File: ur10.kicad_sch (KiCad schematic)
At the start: 0 parts

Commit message: Draw schematic.
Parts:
- added C14: 22u/25V, Capacitor_SMD:C_0805_2012Metric_Pad1.18x1.45mm_HandSolder, symbol Device:C
- added D1, D3: 1N5819, Diode_SMD:D_SOD-123, symbol Diode:1N5819
- added D2: YELLOW, LED_SMD:LED_0805_2012Metric_Pad1.15x1.40mm_HandSolder, symbol Device:LED
- added H1, H2, H3, H4: M3, MountingHole:MountingHole_3.2mm_M3_Pad_Via, symbol Mechanical:MountingHole
- added J1: ~, symbol Connector:Screw_Terminal_01x06
- added J2: ~, TerminalBlock_4Ucon:TerminalBlock_4Ucon_1x03_P3.50mm_Horizontal, symbol Connector:Screw_Terminal_01x03
- added K1: TNA-2C-12-05-L, Relay_THT:Relay_DPDT_Schrack-RT2-FormC_RM5mm, symbol Relay:Relay_DPDT
- added Q1: AO3401A, Package_TO_SOT_SMD:SOT-23, symbol Transistor_FET:AO3401A
- added R1, R14: 1k, Resistor_SMD:R_0805_2012Metric_Pad1.20x1.40mm_HandSolder, symbol Device:R
- added R11: 10k, Resistor_SMD:R_0805_2012Metric_Pad1.20x1.40mm_HandSolder, symbol Device:R
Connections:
- new net: C14.1, D1.1 (K), Q1.2 (S), R11.1
- new net: Q1.1 (G), R11.2, R14.2
- new net: D2.1 (K), R1.2
- new net: D2.2 (A), D3.1 (K), K1.A1, Q1.3 (D)
- new net 11: J1.5 (Pin_5), K1.11
- new net 12: J1.4 (Pin_4), K1.12
- new net 14: J1.6 (Pin_6), K1.14
- new net 21: J1.2 (Pin_2), K1.21
- new net 22: J1.1 (Pin_1), K1.22
- new net 24: J1.3 (Pin_3), K1.24
- new net CONTROL: J2.3 (Pin_3), R14.1
- new net GND: C14.2, D3.2 (A), J2.2 (Pin_2), K1.A2, R1.1
- new net VCC: D1.2 (A), J2.1 (Pin_1)
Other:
- company: (none) -> Model Railroader Club Brno I – KMŽ Brno I – https://kmz-brno.cz/
- title: (none) -> UR-10 - Universal relay module

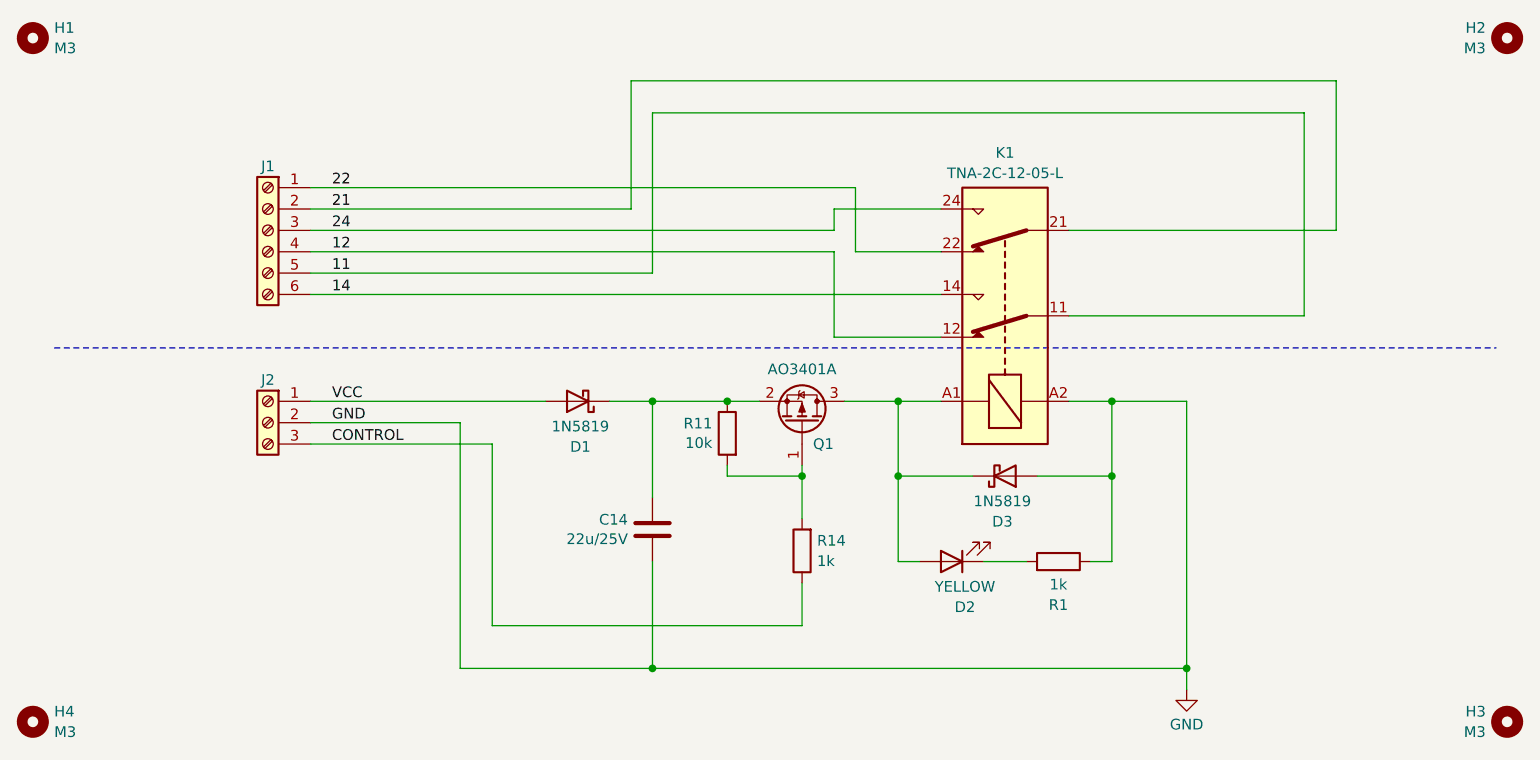
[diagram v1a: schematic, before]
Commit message: Add Q1 bypass, add polarity switch option.
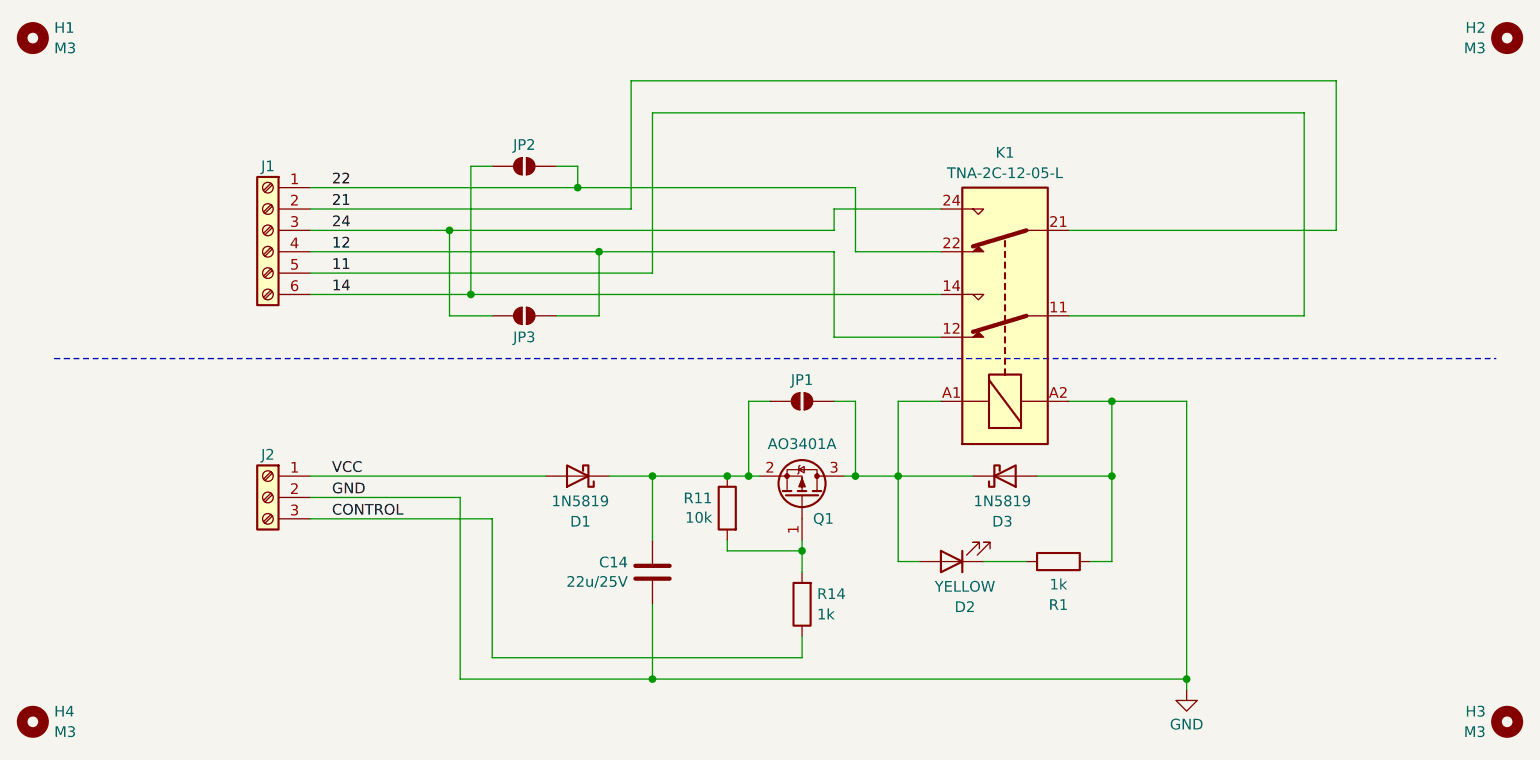
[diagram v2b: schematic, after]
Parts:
- added JP1, JP2, JP3: ~, symbol Jumper:SolderJumper_2_Open
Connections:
- net 12: now also JP3.2 (B)
- net 14: now also JP2.1 (A)
- net 22: now also JP2.2 (B)
- net 24: now also JP3.1 (A)
- net at C14.1, D1.1 (K), Q1.2 (S)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: now also JP1.1 (A)
- net at D2.2 (A), D3.1 (K), K1.A1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: now also JP1.2 (B)
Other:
- moved on the sheet: C14, D1, J2, Q1, R11, R14

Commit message: Wire PCB.
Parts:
- J1: footprint (none) -> TerminalBlock_Euroclamp:MVE252-5-V-3x
- JP1: renamed from JP2; footprint (none) -> Jumper:SolderJumper-2_P1.3mm_Open_RoundedPad1.0x1.5mm
- JP2: renamed from JP3; footprint (none) -> Jumper:SolderJumper-2_P1.3mm_Open_RoundedPad1.0x1.5mm
- JP3: renamed from JP1; footprint (none) -> Jumper:SolderJumper-2_P1.3mm_Open_RoundedPad1.0x1.5mm
- Q1: footprint Package_TO_SOT_SMD:SOT-23 -> Package_TO_SOT_SMD:SOT-23_Handsoldering
- renumbered C14 to C1, D3 to D2, D2 to D3, H4 to H3, H3 to H4, R11 to R1, R1 to R2, R14 to R3
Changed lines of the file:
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@@
 		(on_board yes)
 		(dnp no)
-		(property "Reference" "R11"
+		(property "Reference" "R1"
 			(at 97.282 72.4916 0)
 			(effects
@@
 			(project "ur10"
 				(path "/23315eab-0fca-4b67-95b2-d836b4cb453c"
-					(reference "R11")
+					(reference "R1")
 					(unit 1)
 				)
@@
 		(dnp no)
 		(fields_autoplaced yes)
-		(property "Reference" "#PWR02"
+		(property "Reference" "#PWR01"
 			(at 153.67 101.6 0)
 			(effects
@@
 			(project ""
 				(path "/23315eab-0fca-4b67-95b2-d836b4cb453c"
-					(reference "#PWR02")
+					(reference "#PWR01")
 					(unit 1)
 				)
@@
 		(dnp no)
 		(fields_autoplaced yes)
-		(property "Reference" "R14"
+		(property "Reference" "R3"
 			(at 109.728 83.8778 0)
 			(effects
@@
 			(project "ur10"
 				(path "/23315eab-0fca-4b67-95b2-d836b4cb453c"
-					(reference "R14")
+					(reference "R3")
 					(unit 1)
 				)
@@
 			)
 		)
-		(property "Footprint" ""
+		(property "Footprint" "TerminalBlock_Euroclamp:MVE252-5-V-3x"
 			(at 44.45 40.64 0)
 			(effects
@@
 		(on_board yes)
 		(dnp no)
-		(property "Reference" "D2"
+		(property "Reference" "D3"
 			(at 127.3175 85.4245 0)
 			(effects
@@
 			(project "ur10"
 				(path "/23315eab-0fca-4b67-95b2-d836b4cb453c"
-					(reference "D2")
+					(reference "D3")
 					(unit 1)
 				)
@@
 		(on_board yes)
 		(dnp no)
-		(property "Reference" "H3"
+		(property "Reference" "H4"
 			(at 189.23 97.8478 0)
 			(effects
@@
 			(project "ur10"
 				(path "/23315eab-0fca-4b67-95b2-d836b4cb453c"
-					(reference "H3")
+					(reference "H4")
 					(unit 1)
 				)
@@
 		(on_board yes)
 		(dnp no)
-		(property "Reference" "JP2"
+		(property "Reference" "JP1"
 			(at 74.93 30.48 0)
 			(effects
@@
 			)
 		)
-		(property "Footprint" ""
+		(property "Footprint" "Jumper:SolderJumper-2_P1.3mm_Open_RoundedPad1.0x1.5mm"
 			(at 74.93 33.02 0)
 			(effects
@@
 			(project ""
 				(path "/23315eab-0fca-4b67-95b2-d836b4cb453c"
-					(reference "JP2")
+					(reference "JP1")
 					(unit 1)
 				)
@@
 			)
 		)
-		(property "Footprint" "Package_TO_SOT_SMD:SOT-23"
+		(property "Footprint" "Package_TO_SOT_SMD:SOT-23_Handsoldering"
 			(at 106.045 67.31 0)
 			(effects
@@
 		(on_board yes)
 		(dnp no)
-		(property "Reference" "H4"
+		(property "Reference" "H3"
 			(at 19.05 97.8478 0)
 			(effects
@@
 			(project "ur10"
 				(path "/23315eab-0fca-4b67-95b2-d836b4cb453c"
-					(reference "H4")
+					(reference "H3")
 					(unit 1)
 				)
@@
 		(on_board yes)
 		(dnp no)
-		(property "Reference" "C14"
+		(property "Reference" "C1"
 			(at 87.249 80.1116 0)
 			(effects
@@
 			(project "ur10"
 				(path "/23315eab-0fca-4b67-95b2-d836b4cb453c"
-					(reference "C14")
+					(reference "C1")
 					(unit 1)
 				)
@@
 		(on_board yes)
 		(dnp no)
-		(property "Reference" "JP1"
+		(property "Reference" "JP3"
 			(at 107.95 58.42 0)
 			(effects
@@
 			)
 		)
-		(property "Footprint" ""
+		(property "Footprint" "Jumper:SolderJumper-2_P1.3mm_Open_RoundedPad1.0x1.5mm"
 			(at 107.95 60.96 0)
 			(effects
@@
 			(project ""
 				(path "/23315eab-0fca-4b67-95b2-d836b4cb453c"
-					(reference "JP1")
+					(reference "JP3")
 					(unit 1)
 				)
@@
 		(on_board yes)
 		(dnp no)
-		(property "Reference" "R1"
+		(property "Reference" "R2"
 			(at 138.43 85.1705 90)
 			(effects
@@
 			(project "ur10"
 				(path "/23315eab-0fca-4b67-95b2-d836b4cb453c"
-					(reference "R1")
+					(reference "R2")
 					(unit 1)
 				)
@@
 		(on_board yes)
 		(dnp no)
-		(property "Reference" "JP3"
+		(property "Reference" "JP2"
 			(at 74.93 53.34 0)
 			(effects
@@
 			)
 		)
-		(property "Footprint" ""
+		(property "Footprint" "Jumper:SolderJumper-2_P1.3mm_Open_RoundedPad1.0x1.5mm"
 			(at 74.93 50.8 0)
 			(effects
@@
 			(project "ur10"
 				(path "/23315eab-0fca-4b67-95b2-d836b4cb453c"
-					(reference "JP3")
+					(reference "JP2")
 					(unit 1)
 				)
@@
 		(on_board yes)
 		(dnp no)
-		(property "Reference" "D3"
+		(property "Reference" "D2"
 			(at 131.7625 75.2645 0)
 			(effects
@@
 			(project "ur10"
 				(path "/23315eab-0fca-4b67-95b2-d836b4cb453c"
-					(reference "D3")
-					(unit 1)
-				)
+					(reference "D2")
+					(unit 1)
+				)

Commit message: Use THT jumpers instead of solder jumpers.
Reason: they are visible from top side.
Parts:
- JP1, JP2, JP3: footprint Jumper:SolderJumper-2_P1.3mm_Open_RoundedPad1.0x1.5mm -> Connector_PinHeader_2.54mm:PinHeader_1x02_P2.54mm_Vertical; symbol Jumper:SolderJumper_2_Open -> Jumper:Jumper_2_Open; now in the parts list
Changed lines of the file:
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@@
+	(wire
+		(pts
+			(xy 80.01 33.02) (xy 81.28 33.02)
+		)
+		(stroke
+			(width 0)
+			(type default)
+		)
+	)
 	(wire
 		(pts
@@
 	(wire
 		(pts
+			(xy 80.01 50.8) (xy 83.82 50.8)
+		)
+		(stroke
+			(width 0)
+			(type default)
+		)
+	)
+	(wire
+		(pts
 			(xy 67.31 72.39) (xy 67.31 93.98)
 		)
@@
 	(wire
 		(pts
-			(xy 78.74 33.02) (xy 81.28 33.02)
-		)
-		(stroke
-			(width 0)
-			(type default)
-		)
-	)
-	(wire
-		(pts
 			(xy 144.78 60.96) (xy 153.67 60.96)
 		)
@@
 	(wire
 		(pts
+			(xy 68.58 33.02) (xy 69.85 33.02)
+		)
+		(stroke
+			(width 0)
+			(type default)
+		)
+	)
+	(wire
+		(pts
+			(xy 113.03 60.96) (xy 114.3 60.96)
+		)
+		(stroke
+			(width 0)
+			(type default)
+		)
+	)
+	(wire
+		(pts
 			(xy 71.12 91.44) (xy 71.12 74.93)
 		)
@@
 	(wire
 		(pts
-			(xy 111.76 60.96) (xy 114.3 60.96)
-		)
-		(stroke
-			(width 0)
-			(type default)
-		)
-	)
-	(wire
-		(pts
 			(xy 49.53 35.56) (xy 81.28 35.56)
 		)
@@
 	(wire
 		(pts
-			(xy 78.74 50.8) (xy 83.82 50.8)
-		)
-		(stroke
-			(width 0)
-			(type default)
-		)
-	)
-	(wire
-		(pts
 			(xy 111.76 40.64) (xy 111.76 38.1)
 		)
@@
 	(wire
 		(pts
+			(xy 66.04 50.8) (xy 69.85 50.8)
+		)
+		(stroke
+			(width 0)
+			(type default)
+		)
+	)
+	(wire
+		(pts
 			(xy 114.3 43.18) (xy 124.46 43.18)
 		)
@@
 	(wire
 		(pts
-			(xy 104.14 60.96) (xy 101.6 60.96)
-		)
-		(stroke
-			(width 0)
-			(type default)
-		)
-	)
-	(wire
-		(pts
 			(xy 90.17 93.98) (xy 153.67 93.98)
 		)
@@
 	(wire
 		(pts
+			(xy 101.6 60.96) (xy 102.87 60.96)
+		)
+		(stroke
+			(width 0)
+			(type default)
+		)
+	)
+	(wire
+		(pts
 			(xy 67.31 93.98) (xy 90.17 93.98)
 		)
@@
 	(wire
 		(pts
-			(xy 71.12 50.8) (xy 66.04 50.8)
-		)
-		(stroke
-			(width 0)
-			(type default)
-		)
-	)
-	(wire
-		(pts
 			(xy 49.53 48.26) (xy 68.58 48.26)
-		)
-		(stroke
-			(width 0)
-			(type default)
-		)
-	)
-	(wire
-		(pts
-			(xy 71.12 33.02) (xy 68.58 33.02)
 		)
 		(stroke
@@
 	)
 	(symbol
-		(lib_id "Jumper:SolderJumper_2_Open")
+		(lib_id "Jumper:Jumper_2_Open")
 		(at 74.93 33.02 0)
 		(unit 1)
 		(exclude_from_sim no)
-		(in_bom no)
+		(in_bom yes)
 		(on_board yes)
 		(dnp no)
 		(property "Reference" "JP1"
-			(at 74.93 30.48 0)
+			(at 74.93 29.845 0)
 			(effects
 				(font
@@
 			)
 		)
-		(property "Footprint" "Jumper:SolderJumper-2_P1.3mm_Open_RoundedPad1.0x1.5mm"
+		(property "Footprint" "Connector_PinHeader_2.54mm:PinHeader_1x02_P2.54mm_Vertical"
 			(at 74.93 33.02 0)
 			(effects
@@
 			)
 		)
-		(property "Description" "Solder Jumper, 2-pole, open"
+		(property "Description" "Jumper, 2-pole, open"
 			(at 74.93 33.02 0)
 			(effects
@@
 	)
 	(symbol
-		(lib_id "Jumper:SolderJumper_2_Open")
+		(lib_id "Jumper:Jumper_2_Open")
 		(at 107.95 60.96 0)
 		(unit 1)
 		(exclude_from_sim no)
-		(in_bom no)
+		(in_bom yes)
 		(on_board yes)
 		(dnp no)
 		(property "Reference" "JP3"
-			(at 107.95 58.42 0)
+			(at 107.95 57.785 0)
 			(effects
 				(font
@@
 			)
 		)
-		(property "Footprint" "Jumper:SolderJumper-2_P1.3mm_Open_RoundedPad1.0x1.5mm"
+		(property "Footprint" "Connector_PinHeader_2.54mm:PinHeader_1x02_P2.54mm_Vertical"
 			(at 107.95 60.96 0)
 			(effects
@@
 			)
 		)
-		(property "Description" "Solder Jumper, 2-pole, open"
+		(property "Description" "Jumper, 2-pole, open"
 			(at 107.95 60.96 0)
 			(effects
@@
 	)
 	(symbol
-		(lib_id "Jumper:SolderJumper_2_Open")
+		(lib_id "Jumper:Jumper_2_Open")
 		(at 74.93 50.8 0)
 		(mirror x)
 		(unit 1)
 		(exclude_from_sim no)
-		(in_bom no)
+		(in_bom yes)
 		(on_board yes)
 		(dnp no)
 		(property "Reference" "JP2"
-			(at 74.93 53.34 0)
+			(at 74.93 53.975 0)
 			(effects
 				(font
@@
 			)
 		)
-		(property "Footprint" "Jumper:SolderJumper-2_P1.3mm_Open_RoundedPad1.0x1.5mm"
+		(property "Footprint" "Connector_PinHeader_2.54mm:PinHeader_1x02_P2.54mm_Vertical"
 			(at 74.93 50.8 0)
 			(effects
@@
 			)
 		)
-		(property "Description" "Solder Jumper, 2-pole, open"
+		(property "Description" "Jumper, 2-pole, open"
 			(at 74.93 50.8 0)
 			(effects

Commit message: Use 4k7 resistor for yellow LED.
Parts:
- R2: value 1k -> 4k7
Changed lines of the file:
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@@
 			)
 		)
-		(property "Value" "1k"
+		(property "Value" "4k7"
 			(at 138.43 82.7462 90)
 			(effects
